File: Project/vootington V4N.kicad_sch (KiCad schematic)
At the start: 118 parts, among them U4 SLSS49E-3, U5 SLSS49E-3

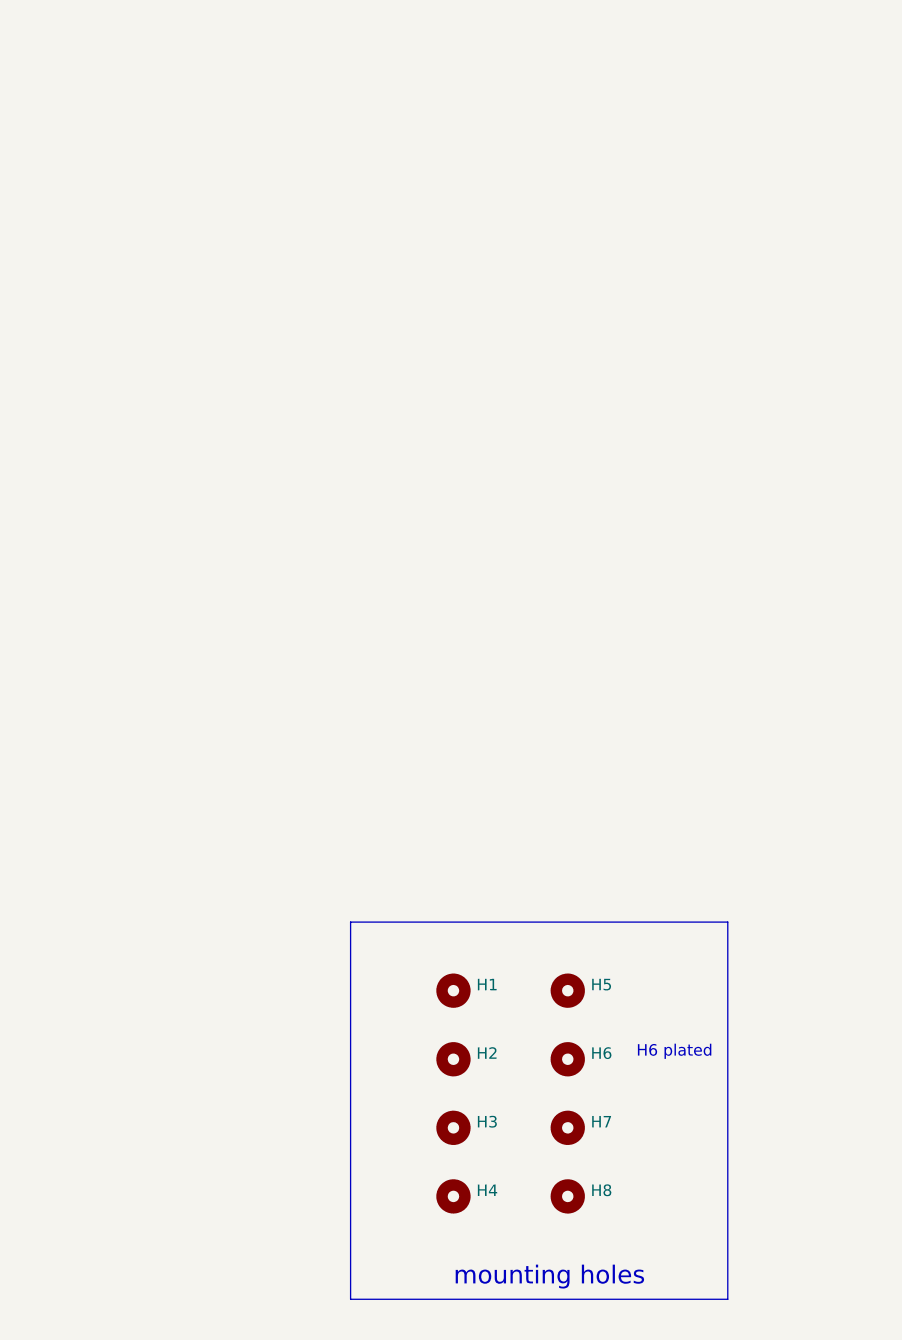
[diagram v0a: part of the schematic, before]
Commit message: created plates and production files for protos
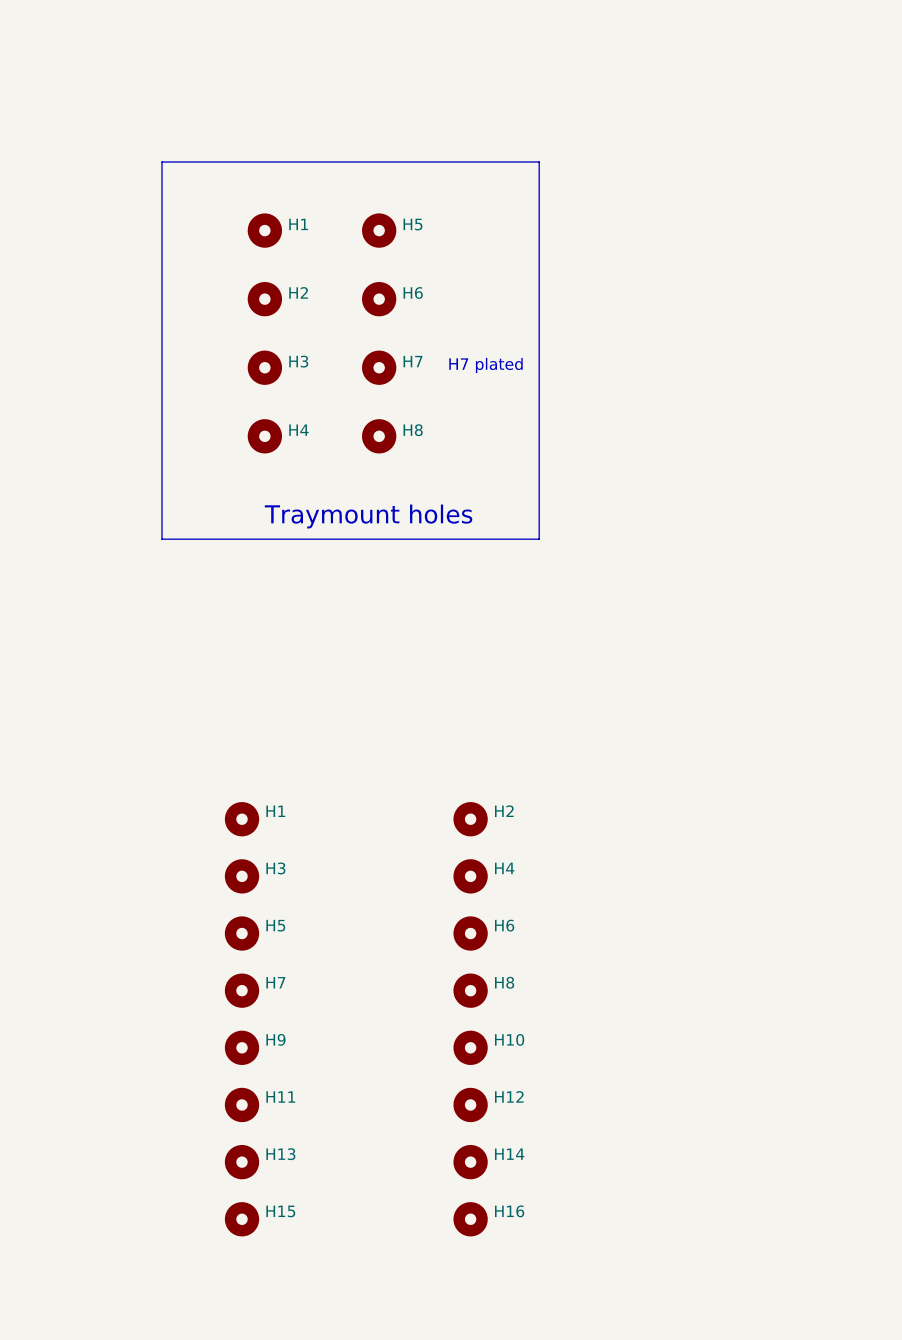
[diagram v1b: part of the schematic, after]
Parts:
- added H1, H10, H11, H12, H13, H14, H15, H16, H2, H3, H4, H5, H6, H7, H8, H9: MountingHole, cipulot_parts:HOLE_M2, symbol Mechanical:MountingHole
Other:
- note added: "H7 plated"
- note added: "Traymount holes"
- note removed: "H6 plated"
- note removed: "mounting holes"
- moved on the sheet: H1, H2, H3, H4, H5, H6, H7, H8
